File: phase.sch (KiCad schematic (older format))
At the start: 29 parts, among them U4 INA240A1PW, U5 UCC21520DW

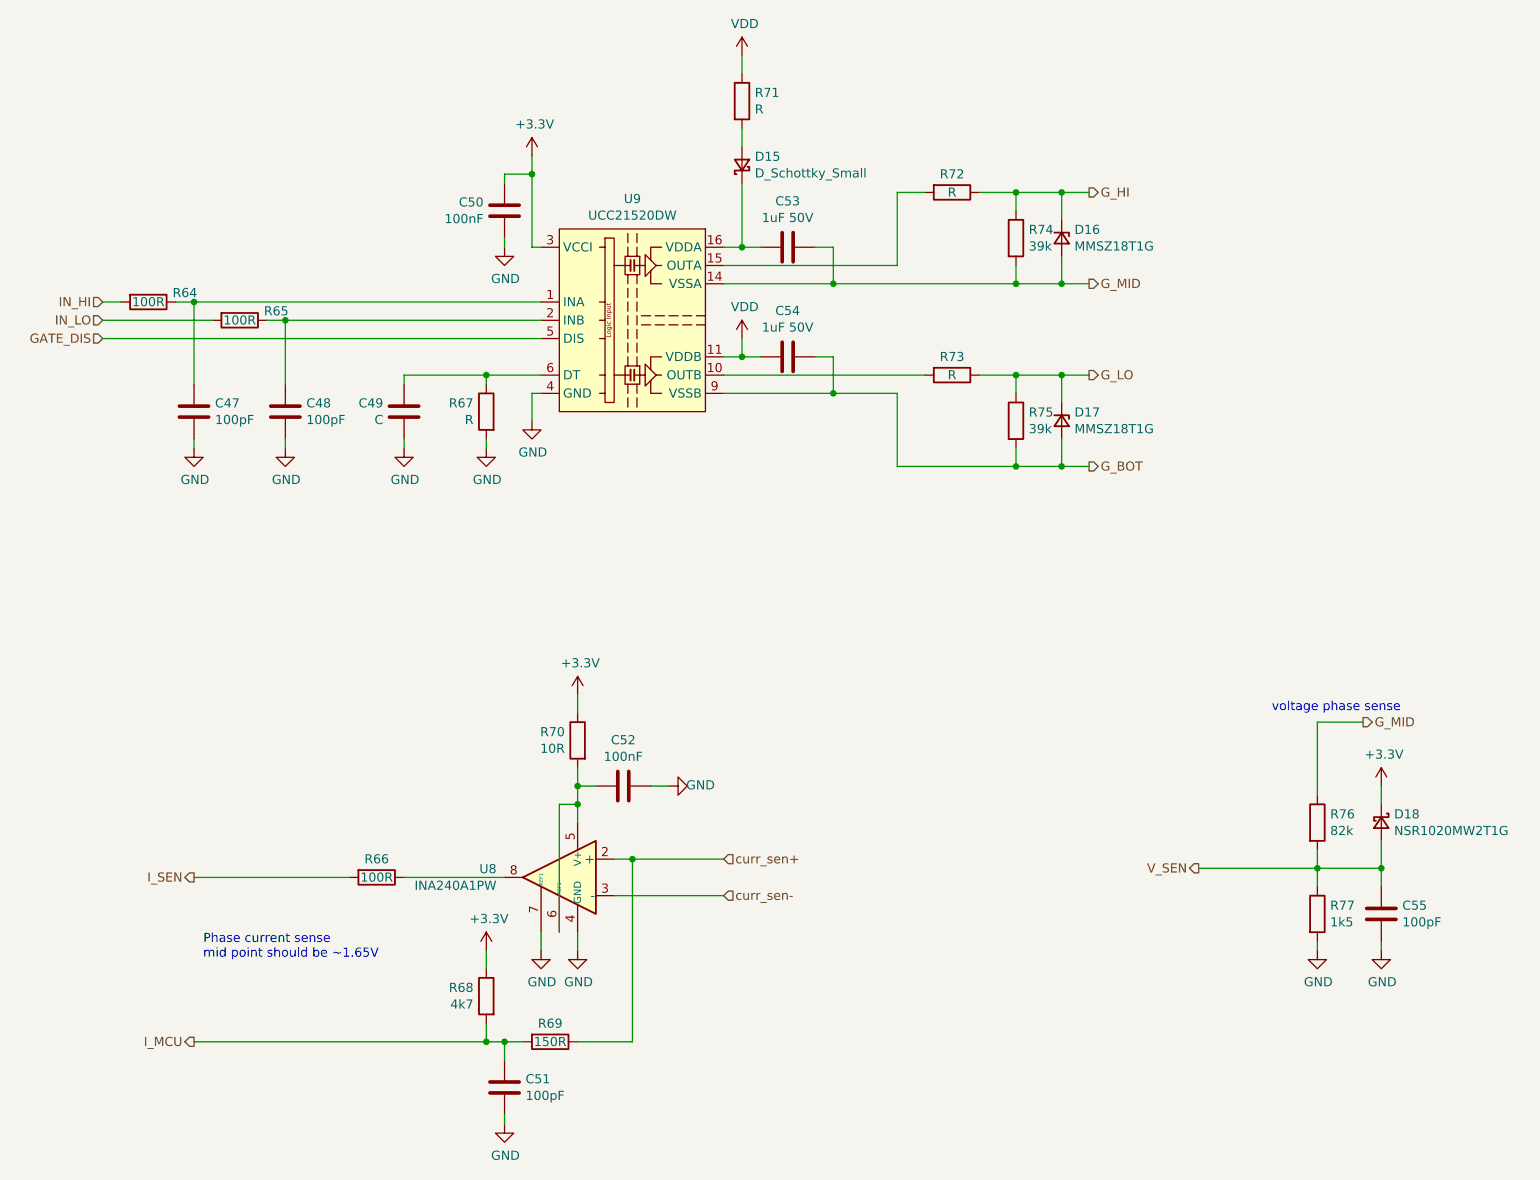
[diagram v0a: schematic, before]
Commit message: Minor updates
Tweaking the README.md
Removing F303 op-amp circuitry.
Re-arranging INA240 circuit
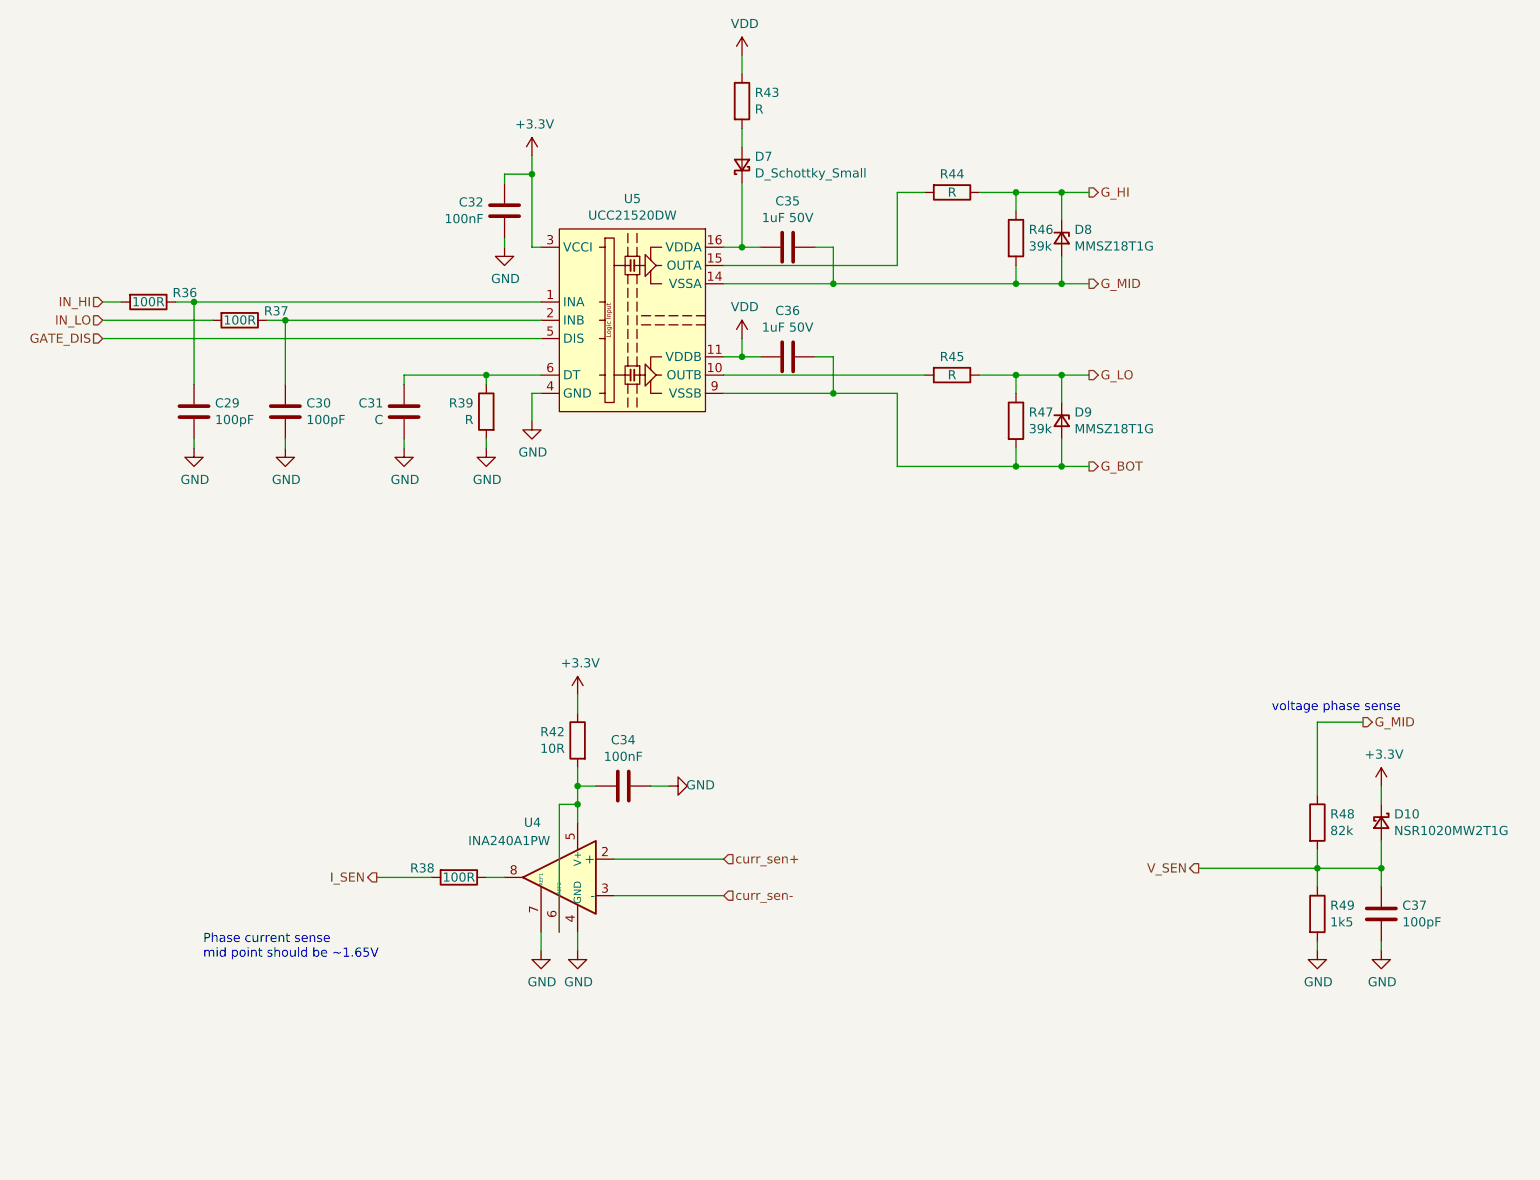
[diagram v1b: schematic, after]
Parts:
- removed C33: 100pF, Capacitor_SMD:C_0402_1005Metric, symbol Device:C
- removed R40: 4k7, symbol Device:R
- removed R41: 150R, symbol Device:R
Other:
- moved on the sheet: R38

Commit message: Adding some test points
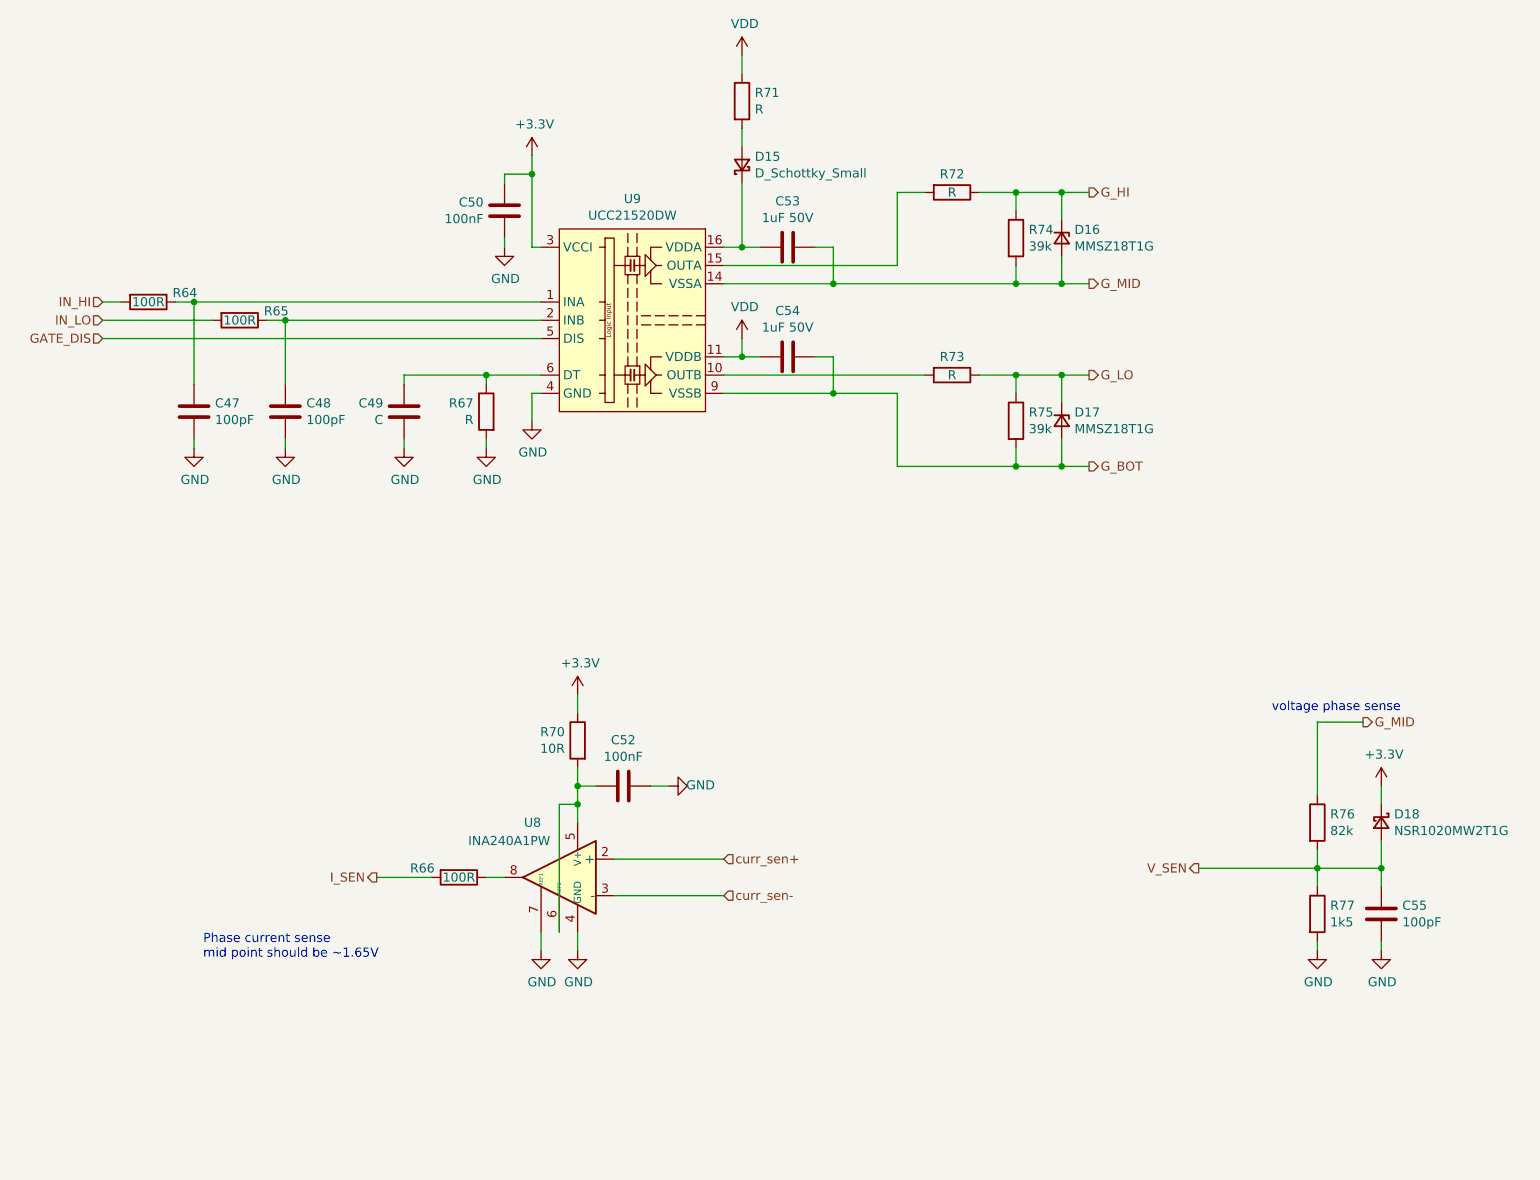
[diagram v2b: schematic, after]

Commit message: Assigned all footprints
Began initial placement
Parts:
- C31: footprint (none) -> Capacitor_SMD:C_0603_1608Metric
- C32: footprint Capacitor_SMD:C_0603_1608Metric -> Capacitor_SMD:C_0402_1005Metric
- C34: footprint (none) -> Capacitor_SMD:C_0402_1005Metric
- C35, C36: footprint (none) -> Capacitor_SMD:C_0805_2012Metric
- D7: footprint (none) -> Diode_SMD:D_SMB
- R39: footprint Resistor_SMD:R_0402_1005Metric -> Resistor_SMD:R_0603_1608Metric
- R43, R44, R45: footprint Resistor_SMD:R_0402_1005Metric -> Resistor_SMD:R_0805_2012Metric
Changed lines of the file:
@@
 $Descr A4 11693 8268
 encoding utf-8
-Sheet 3 5
+Sheet 5 5
 Title "MESC_IMS_ESC"
 Date "2021-04-10"
@@
 F 0 "C50" H 4885 1896 50  0000 R CNN
 F 1 "100nF" H 4885 1805 50  0000 R CNN
-F 2 "Capacitor_SMD:C_0603_1608Metric" H 5038 1700 50  0001 C CNN
+F 2 "Capacitor_SMD:C_0402_1005Metric" H 5038 1700 50  0001 C CNN
 F 3 "~" H 5000 1850 50  0001 C CNN
 	1    5000 1850
@@
 F 0 "R67" H 4970 2996 50  0000 L CNN
 F 1 "R" H 4970 2905 50  0000 L CNN
-F 2 "Resistor_SMD:R_0402_1005Metric" V 4830 2950 50  0001 C CNN
+F 2 "Resistor_SMD:R_0603_1608Metric" V 4830 2950 50  0001 C CNN
 F 3 "~" H 4900 2950 50  0001 C CNN
 	1    4900 2950
@@
 F 0 "C49" H 4336 2904 50  0000 R CNN
 F 1 "C" H 4336 2995 50  0000 R CNN
-F 2 "" H 4488 2800 50  0001 C CNN
+F 2 "Capacitor_SMD:C_0603_1608Metric" H 4488 2800 50  0001 C CNN
 F 3 "~" H 4450 2950 50  0001 C CNN
 	1    4450 2950
@@
 F 0 "C53" V 6298 2050 50  0000 C CNN
 F 1 "1uF 50V" V 6389 2050 50  0000 C CNN
-F 2 "" H 6588 1900 50  0001 C CNN
+F 2 "Capacitor_SMD:C_0805_2012Metric" H 6588 1900 50  0001 C CNN
 F 3 "~" H 6550 2050 50  0001 C CNN
 	1    6550 2050
@@
 F 0 "C54" V 6298 2650 50  0000 C CNN
 F 1 "1uF 50V" V 6389 2650 50  0000 C CNN
-F 2 "" H 6588 2500 50  0001 C CNN
+F 2 "Capacitor_SMD:C_0805_2012Metric" H 6588 2500 50  0001 C CNN
 F 3 "~" H 6550 2650 50  0001 C CNN
 	1    6550 2650
@@
 F 0 "D15" V 6346 1530 50  0000 R CNN
 F 1 "D_Schottky_Small" V 6255 1530 50  0000 R CNN
-F 2 "" V 6300 1600 50  0001 C CNN
+F 2 "Diode_SMD:D_SMB" V 6300 1600 50  0001 C CNN
 F 3 "~" V 6300 1600 50  0001 C CNN
 	1    6300 1600
@@
 F 0 "R71" H 6370 1296 50  0000 L CNN
 F 1 "R" H 6370 1205 50  0000 L CNN
-F 2 "Resistor_SMD:R_0402_1005Metric" V 6230 1250 50  0001 C CNN
+F 2 "Resistor_SMD:R_0805_2012Metric" V 6230 1250 50  0001 C CNN
 F 3 "~" H 6300 1250 50  0001 C CNN
 	1    6300 1250
@@
 F 0 "R73" V 7350 2750 50  0000 C CNN
 F 1 "R" V 7450 2750 50  0000 C CNN
-F 2 "Resistor_SMD:R_0402_1005Metric" V 7380 2750 50  0001 C CNN
+F 2 "Resistor_SMD:R_0805_2012Metric" V 7380 2750 50  0001 C CNN
 F 3 "~" H 7450 2750 50  0001 C CNN
 	1    7450 2750
@@
 F 0 "R72" V 7350 1750 50  0000 C CNN
 F 1 "R" V 7450 1750 50  0000 C CNN
-F 2 "Resistor_SMD:R_0402_1005Metric" V 7380 1750 50  0001 C CNN
+F 2 "Resistor_SMD:R_0805_2012Metric" V 7380 1750 50  0001 C CNN
 F 3 "~" H 7450 1750 50  0001 C CNN
 	1    7450 1750
@@
 F 0 "C52" V 5398 5000 50  0000 C CNN
 F 1 "100nF" V 5489 5000 50  0000 C CNN
-F 2 "" H 5688 4850 50  0001 C CNN
+F 2 "Capacitor_SMD:C_0402_1005Metric" H 5688 4850 50  0001 C CNN
 F 3 "~" H 5650 5000 50  0001 C CNN
 	1    5650 5000
